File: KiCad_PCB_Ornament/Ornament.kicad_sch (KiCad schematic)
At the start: 55 parts, among them J1 Conn_01x04_Pin, J2 Conn_01x04_Pin, Q1 TEMT6200FX01, SW1 SW_Push, SW2 SW_SPDT, U1 ATtiny414-SS, U2 INA190A3IDDFR

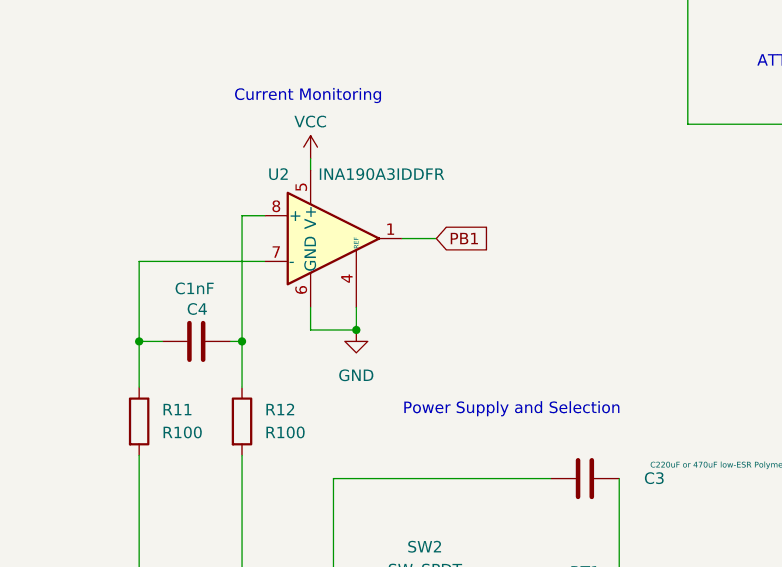
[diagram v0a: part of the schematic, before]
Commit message: PCB updates to fix current sense amplifier layout and complete BOM
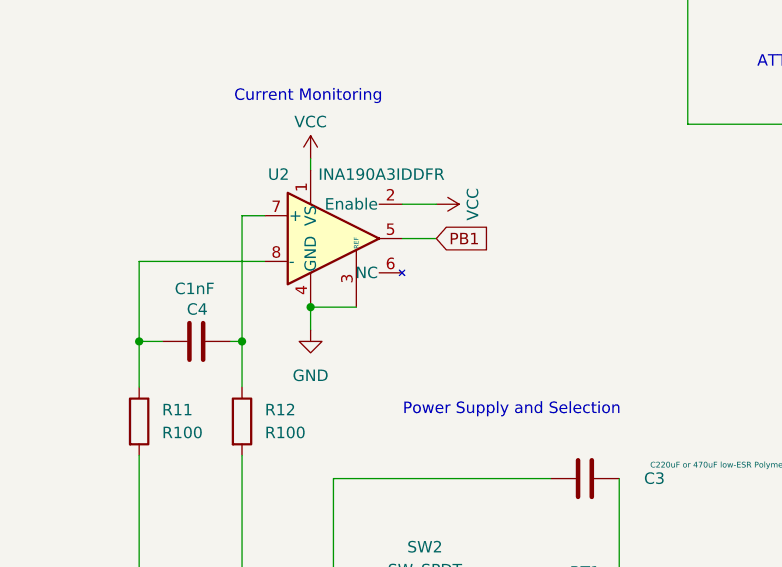
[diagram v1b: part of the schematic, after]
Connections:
- net GND: now also U2.3 (REF); no longer U2.6 (GND)
- net PB1: now also U2.5; no longer U2.1
- net VCC: now also U2.1 (VS), U2.2 (Enable); no longer U2.5 (V+)
- net at C4.1, R11.1: now also U2.8 (-); no longer U2.7 (-)
- net at C4.2, R12.1: now also U2.7 (+); no longer U2.8 (+)
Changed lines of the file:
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@@
 	)
 	(junction
-		(at 54.61 149.86)
+		(at 49.53 147.32)
 		(diameter 0)
 		(color 0 0 0 0)
@@
 	(wire
 		(pts
+			(xy 49.53 147.32) (xy 49.53 149.86)
+		)
+		(stroke
+			(width 0)
+			(type default)
+		)
+	)
+	(wire
+		(pts
 			(xy 242.57 39.37) (xy 242.57 46.99)
 		)
@@
 	(wire
 		(pts
+			(xy 59.69 135.89) (xy 63.5 135.89)
+		)
+		(stroke
+			(width 0)
+			(type default)
+		)
+	)
+	(wire
+		(pts
 			(xy 91.44 127) (xy 125.73 127)
 		)
@@
 	(wire
 		(pts
+			(xy 49.53 147.32) (xy 54.61 147.32)
+		)
+		(stroke
+			(width 0)
+			(type default)
+		)
+	)
+	(wire
+		(pts
 			(xy 48.26 82.55) (xy 48.26 90.17)
 		)
@@
 	(wire
 		(pts
-			(xy 54.61 147.32) (xy 54.61 149.86)
-		)
-		(stroke
-			(width 0)
-			(type default)
-		)
-	)
-	(wire
-		(pts
 			(xy 33.02 33.02) (xy 50.8 33.02)
 		)
@@
 	(wire
 		(pts
-			(xy 49.53 149.86) (xy 54.61 149.86)
-		)
-		(stroke
-			(width 0)
-			(type default)
-		)
-	)
-	(wire
-		(pts
 			(xy 196.85 39.37) (xy 196.85 46.99)
 		)
@@
 		)
 	)
-	(wire
-		(pts
-			(xy 49.53 147.32) (xy 49.53 149.86)
-		)
-		(stroke
-			(width 0)
-			(type default)
-		)
-	)
 	(global_label "PA1"
 		(shape input)
@@
 	)
 	(symbol
+		(lib_id "power:VCC")
+		(at 63.5 135.89 270)
+		(unit 1)
+		(exclude_from_sim no)
+		(in_bom yes)
+		(on_board yes)
+		(dnp no)
+		(property "Reference" "#PWR014"
+			(at 59.69 135.89 0)
+			(effects
+				(font
+					(size 1.27 1.27)
+				)
+				(hide yes)
+			)
+		)
+		(property "Value" "VCC"
+			(at 67.564 135.89 0)
+			(effects
+				(font
+					(size 1.27 1.27)
+				)
+			)
+		)
+		(property "Footprint" ""
+			(at 63.5 135.89 0)
+			(effects
+				(font
+					(size 1.27 1.27)
+				)
+				(hide yes)
+			)
+		)
+		(property "Datasheet" ""
+			(at 63.5 135.89 0)
+			(effects
+				(font
+					(size 1.27 1.27)
+				)
+				(hide yes)
+			)
+		)
+		(property "Description" "Power symbol creates a global label with name \"VCC\""
+			(at 63.5 135.89 0)
+			(effects
+				(font
+					(size 1.27 1.27)
+				)
+				(hide yes)
+			)
+		)
+		(pin "1"
+		)
+		(instances
+			(project "Ornament"
+				(path "/1062e0da-9b26-4bb7-aad3-a0048a4e1f8e"
+					(reference "#PWR014")
+					(unit 1)
+				)
+			)
+		)
+	)
+	(symbol
 		(lib_id "power:GND")
-		(at 54.61 149.86 0)
+		(at 49.53 149.86 0)
 		(unit 1)
 		(exclude_from_sim no)
@@
 		(fields_autoplaced yes)
 		(property "Reference" "#PWR09"
-			(at 54.61 156.21 0)
+			(at 49.53 156.21 0)
 			(effects
 				(font
@@
 		)
 		(property "Value" "GND"
-			(at 54.61 154.94 0)
+			(at 49.53 154.94 0)
 			(effects
 				(font
@@
 		)
 		(property "Footprint" ""
-			(at 54.61 149.86 0)
+			(at 49.53 149.86 0)
 			(effects
 				(font
@@
 		)
 		(property "Datasheet" ""
-			(at 54.61 149.86 0)
+			(at 49.53 149.86 0)
 			(effects
 				(font
@@
 		)
 		(property "Description" "Power symbol creates a global label with name \"GND\" , ground"
-			(at 54.61 149.86 0)
+			(at 49.53 149.86 0)
 			(effects
 				(font
@@
 		(pin "1"
 		)
+		(pin "3"
+		)
+		(pin "2"
+		)
 		(instances
